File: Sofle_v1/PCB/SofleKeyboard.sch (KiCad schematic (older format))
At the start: 85 parts, among them J1 LED, J2 4PIN, J3 OLED, P1 i2c_pin, P2 i2c_pin, SW1 SW_PUSH, SW10 SW_PUSH, SW11 SW_PUSH, SW12 SW_PUSH, SW13 SW_PUSH, SW14 SW_PUSH, SW15 SW_PUSH, SW16 SW_PUSH, SW17 SW_PUSH, SW18 SW_PUSH, SW19 SW_PUSH, SW2 SW_PUSH, SW20 SW_PUSH, SW21 SW_PUSH, SW22 SW_PUSH, SW23 SW_PUSH, SW24 SW_PUSH, SW25 Rotary_Encoder_Switch, SW26 SW_PUSH, SW27 SW_PUSH, SW28 SW_PUSH, SW29 SW_PUSH, SW3 SW_PUSH, SW30 SW_PUSH, SW4 SW_PUSH, SW5 SW_PUSH, SW6 SW_PUSH, SW7 SW_PUSH, SW8 SW_PUSH, SW9 SW_PUSH, U1 ProMicro

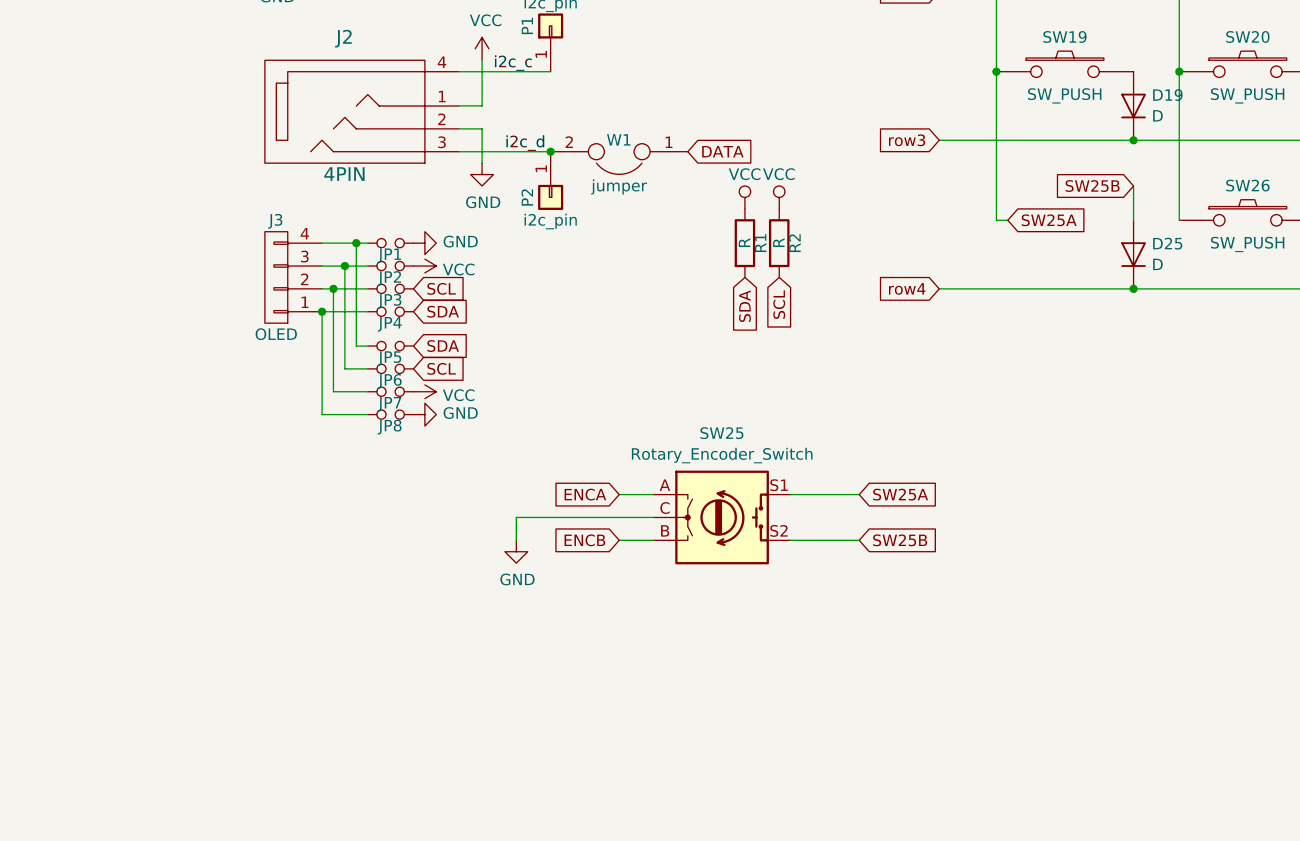
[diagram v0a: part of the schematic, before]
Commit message: Done with the scheme and positioning of the footprints. Started drawing the tracks
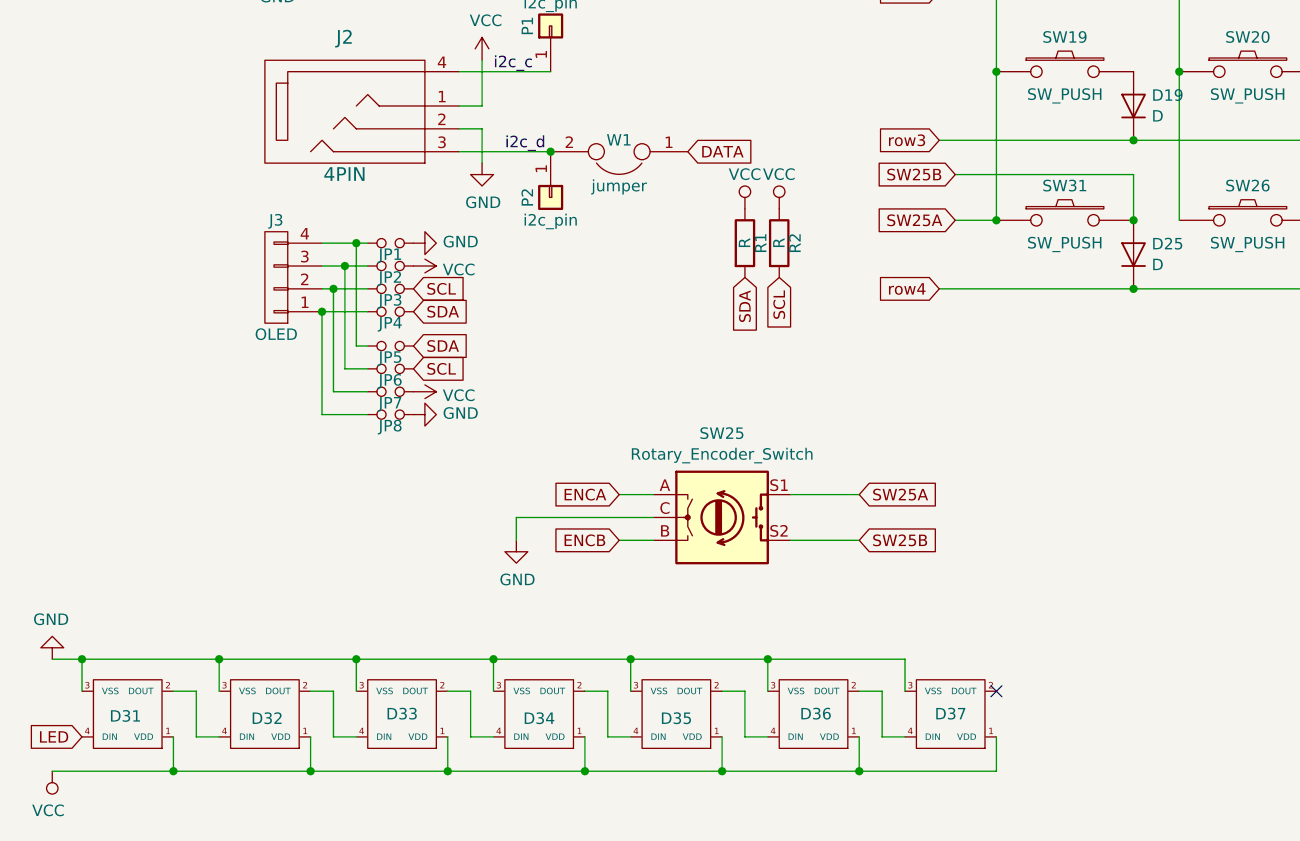
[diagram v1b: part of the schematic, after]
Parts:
- added D31, D32, D33, D34, D35, D36, D37: SK6812MINI, footprints:YS-SK6812MINI-E_backlight, symbol sk6812mini_led:SK6812MINI_LED
- added SW31: SW_PUSH, SofleKeyboard-footprint:CherryMX_Hotswap, symbol SofleKeyboard-rescue:SW_PUSH-Lily58-cache-Lily58_Pro-rescue
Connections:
- net GND: now also D31.3 (VSS), D32.3 (VSS), D33.3 (VSS), D34.3 (VSS), D35.3 (VSS), D36.3 (VSS), D37.3 (VSS)
- net LED: now also D31.4 (DIN)
- net SW25A: now also SW31.1
- net SW25B: now also SW31.2
- net VCC: now also D31.1 (VDD), D32.1 (VDD), D33.1 (VDD), D34.1 (VDD), D35.1 (VDD), D36.1 (VDD), D37.1 (VDD)
- new net: D31.2 (DOUT), D32.4 (DIN)
- new net: D32.2 (DOUT), D33.4 (DIN)
- new net: D33.2 (DOUT), D34.4 (DIN)
- new net: D34.2 (DOUT), D35.4 (DIN)
- new net: D35.2 (DOUT), D36.4 (DIN)
- new net: D36.2 (DOUT), D37.4 (DIN)
- no-connect marks 2 -> 3
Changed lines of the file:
@@
 Wire Wire Line
 	4600 6250 4900 6250
-Text GLabel 5550 4850 2    50   Input ~ 0
+Text GLabel 5320 4850 0    50   Input ~ 0
 SW25A
-Text GLabel 6100 4700 0    50   Input ~ 0
+Text GLabel 5320 4650 0    50   Input ~ 0
 SW25B
-Wire Wire Line
-	6100 4700 6100 4850
-Wire Wire Line
-	5500 4850 5550 4850
 Text GLabel 3850 2500 2    50   Input ~ 0
 ENCA
@@
 Text Label 3300 4200 0    50   ~ 0
 i2c_c
+$Comp
+L sk6812mini_led:SK6812MINI_LED D31
+U 1 1 61DF815A
+P 1700 7010
+F 0 "D31" H 1640 7020 50  0000 L CNN
+F 1 "SK6812MINI" H 1510 7470 50  0001 L CNN
+F 2 "footprints:YS-SK6812MINI-E_backlight" H 1750 6710 50  0001 L TNN
+F 3 "https://cdn-shop.adafruit.com/product-files/2686/SK6812MINI_REV.01-1-2.pdf" H 1800 6635 50  0001 L TNN
+	1    1700 7010
+	-1   0    0    1
+$EndComp
+$Comp
+L sk6812mini_led:SK6812MINI_LED D32
+U 1 1 61DFB69F
+P 2300 7010
+F 0 "D32" H 2220 7030 50  0000 L CNN
+F 1 "SK6812MINI" H 2110 7470 50  0001 L CNN
+F 2 "footprints:YS-SK6812MINI-E_backlight" H 2350 6710 50  0001 L TNN
+F 3 "https://cdn-shop.adafruit.com/product-files/2686/SK6812MINI_REV.01-1-2.pdf" H 2400 6635 50  0001 L TNN
+	1    2300 7010
+	-1   0    0    1
+$EndComp
+$Comp
+L sk6812mini_led:SK6812MINI_LED D33
+U 1 1 61DFE6B6
+P 2900 7010
+F 0 "D33" H 2830 7010 50  0000 L CNN
+F 1 "SK6812MINI" H 2710 7470 50  0001 L CNN
+F 2 "footprints:YS-SK6812MINI-E_backlight" H 2950 6710 50  0001 L TNN
+F 3 "https://cdn-shop.adafruit.com/product-files/2686/SK6812MINI_REV.01-1-2.pdf" H 3000 6635 50  0001 L TNN
+	1    2900 7010
+	-1   0    0    1
+$EndComp
+$Comp
+L sk6812mini_led:SK6812MINI_LED D34
+U 1 1 61E0164B
+P 3500 7010
+F 0 "D34" H 3430 7030 50  0000 L CNN
+F 1 "SK6812MINI" H 3310 7470 50  0001 L CNN
+F 2 "footprints:YS-SK6812MINI-E_backlight" H 3550 6710 50  0001 L TNN
+F 3 "https://cdn-shop.adafruit.com/product-files/2686/SK6812MINI_REV.01-1-2.pdf" H 3600 6635 50  0001 L TNN
+	1    3500 7010
+	-1   0    0    1
+$EndComp
+$Comp
+L sk6812mini_led:SK6812MINI_LED D35
+U 1 1 61E0450F
+P 4100 7010
+F 0 "D35" H 4030 7030 50  0000 L CNN
+F 1 "SK6812MINI" H 3910 7470 50  0001 L CNN
+F 2 "footprints:YS-SK6812MINI-E_backlight" H 4150 6710 50  0001 L TNN
+F 3 "https://cdn-shop.adafruit.com/product-files/2686/SK6812MINI_REV.01-1-2.pdf" H 4200 6635 50  0001 L TNN
+	1    4100 7010
+	-1   0    0    1
+$EndComp
+$Comp
+L sk6812mini_led:SK6812MINI_LED D36
+U 1 1 61E0744A
+P 4700 7010
+F 0 "D36" H 4620 7010 50  0000 L CNN
+F 1 "SK6812MINI" H 4510 7470 50  0001 L CNN
+F 2 "footprints:YS-SK6812MINI-E_backlight" H 4750 6710 50  0001 L TNN
+F 3 "https://cdn-shop.adafruit.com/product-files/2686/SK6812MINI_REV.01-1-2.pdf" H 4800 6635 50  0001 L TNN
+	1    4700 7010
+	-1   0    0    1
+$EndComp
+$Comp
+L sk6812mini_led:SK6812MINI_LED D37
+U 1 1 61E0A91F
+P 5300 7010
+F 0 "D37" H 5230 7010 50  0000 L CNN
+F 1 "SK6812MINI" H 5110 7470 50  0001 L CNN
+F 2 "footprints:YS-SK6812MINI-E_backlight" H 5350 6710 50  0001 L TNN
+F 3 "https://cdn-shop.adafruit.com/product-files/2686/SK6812MINI_REV.01-1-2.pdf" H 5400 6635 50  0001 L TNN
+	1    5300 7010
+	-1   0    0    1
+$EndComp
+$Comp
+L SofleKeyboard-rescue:GND-Lily58-cache-Lily58_Pro-rescue #PWR016
+U 1 1 61E35F4D
+P 1370 6770
+F 0 "#PWR016" H 1370 6520 50  0001 C CNN
+F 1 "GND" H 1375 6597 50  0000 C CNN
+F 2 "" H 1370 6770 50  0001 C CNN
+F 3 "" H 1370 6770 50  0001 C CNN
+	1    1370 6770
+	-1   0    0    1
+$EndComp
+NoConn ~ 5500 6910
+Text GLabel 1500 7110 0    50   Input ~ 0
+LED
+$Comp
+L SofleKeyboard-rescue:VCC-Lily58-cache-Lily58_Pro-rescue #PWR015
+U 1 1 61E6511F
+P 1370 7260
+F 0 "#PWR015" H 1370 7110 50  0001 C CNN
+F 1 "VCC" H 1387 7433 50  0000 C CNN
+F 2 "" H 1370 7260 50  0001 C CNN
+F 3 "" H 1370 7260 50  0001 C CNN
+	1    1370 7260
+	-1   0    0    1
+$EndComp
+Wire Wire Line
+	1370 6770 1500 6770
+Wire Wire Line
+	1900 6910 2000 6910
+Wire Wire Line
+	2000 6910 2000 7110
+Wire Wire Line
+	2000 7110 2100 7110
+Wire Wire Line
+	2500 6910 2600 6910
+Wire Wire Line
+	2600 6910 2600 7110
+Wire Wire Line
+	2600 7110 2700 7110
+Wire Wire Line
+	3100 6910 3200 6910
+Wire Wire Line
+	3200 6910 3200 7110
+Wire Wire Line
+	3200 7110 3300 7110
+Wire Wire Line
+	3700 6910 3800 6910
+Wire Wire Line
+	3800 6910 3800 7110
+Wire Wire Line
+	3800 7110 3900 7110
+Wire Wire Line
+	4300 6910 4400 6910
+Wire Wire Line
+	4400 6910 4400 7110
+Wire Wire Line
+	4400 7110 4500 7110
+Wire Wire Line
+	4900 6910 5000 6910
+Wire Wire Line
+	5000 6910 5000 7110
+Wire Wire Line
+	5000 7110 5100 7110
+Wire Wire Line
+	1500 6910 1500 6770
+Connection ~ 1500 6770
+Wire Wire Line
+	1500 6770 2100 6770
+Wire Wire Line
+	1900 7110 1900 7260
+Wire Wire Line
+	1370 7260 1900 7260
+Connection ~ 1900 7260
+Wire Wire Line
+	1900 7260 2500 7260
+Wire Wire Line
+	2100 6910 2100 6770
+Connection ~ 2100 6770
+Wire Wire Line
+	2100 6770 2700 6770
+Wire Wire Line
+	2500 7110 2500 7260
+Connection ~ 2500 7260
+Wire Wire Line
+	2500 7260 3100 7260
+Wire Wire Line
+	2700 6910 2700 6770
+Connection ~ 2700 6770
+Wire Wire Line
+	2700 6770 3300 6770
+Wire Wire Line
+	3100 7110 3100 7260
+Connection ~ 3100 7260
+Wire Wire Line
+	3100 7260 3700 7260
+Wire Wire Line
+	3300 6910 3300 6770
+Connection ~ 3300 6770
+Wire Wire Line
+	3300 6770 3900 6770
+Wire Wire Line
+	3700 7110 3700 7260
+Connection ~ 3700 7260
+Wire Wire Line
+	3700 7260 4300 7260
+Wire Wire Line
+	3900 6910 3900 6770
+Connection ~ 3900 6770
+Wire Wire Line
+	3900 6770 4500 6770
+Wire Wire Line
+	4300 7110 4300 7260
+Connection ~ 4300 7260
+Wire Wire Line
+	4300 7260 4900 7260
+Wire Wire Line
+	4500 6910 4500 6770
+Connection ~ 4500 6770
+Wire Wire Line
+	4900 7110 4900 7260
+Connection ~ 4900 7260
+Wire Wire Line
+	5100 6770 5100 6910
+Wire Wire Line
+	4500 6770 5100 6770
+Wire Wire Line
+	5500 7260 5500 7110
+Wire Wire Line
+	4900 7260 5500 7260
+$Comp
+L SofleKeyboard-rescue:SW_PUSH-Lily58-cache-Lily58_Pro-rescue SW31
+U 1 1 620025C2
+P 5800 4850
+F 0 "SW31" H 5800 5000 50  0000 C CNN
+F 1 "SW_PUSH" H 5800 4750 50  0000 C CNN
+F 2 "SofleKeyboard-footprint:CherryMX_Hotswap" H 5800 4850 50  0001 C CNN
+F 3 "" H 5800 4850 50  0000 C CNN
+	1    5800 4850
+	1    0    0    -1
+$EndComp
+Wire Wire Line
+	5320 4850 5500 4850
+Connection ~ 5500 4850
+Wire Wire Line
+	5320 4650 6100 4650
+Wire Wire Line
+	6100 4650 6100 4850
+Connection ~ 6100 4850
 $EndSCHEMATC
